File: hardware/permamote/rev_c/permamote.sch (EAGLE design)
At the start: 125 parts, among them J1 TC2030-JLINK-NL, J5 MICRO_USB_B_HIROSE_ZX62R-B-5P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, Q1 PMDXB950UPEL, Q10 PMDXB950UPEL, Q2 PMDXB950UPEL, Q3 PMDXB950UPEL, Q4 PMDXB950UPEL, Q5 PMDXB950UPEL, Q6 PMDXB950UPEL, Q7 PMDXB950UPEL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

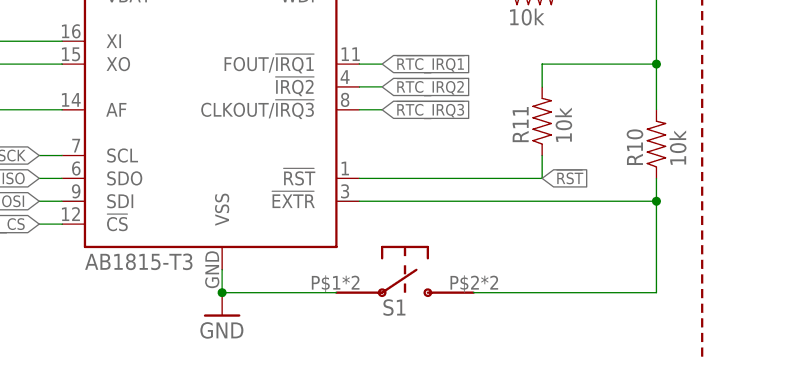
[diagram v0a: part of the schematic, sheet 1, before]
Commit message: Change button, fixes #4
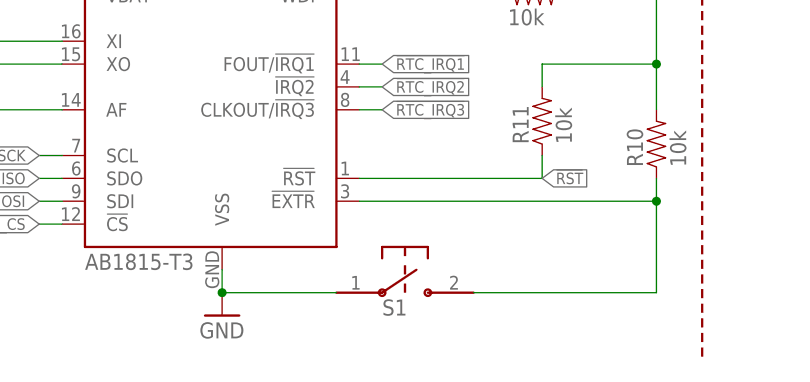
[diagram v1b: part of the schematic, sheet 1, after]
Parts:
- S1: value EVQP2 -> B3U-1000P; device switches:EVQP2 -> switches:B3U-1000P; MPN EVQ-P2K02Q -> (none)
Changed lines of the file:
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@@
 <part name="A2" library="chips" deviceset="ANT3216A063R2400A" device=""/>
 <part name="GND30" library="supply1" library_urn="urn:adsk.eagle:library:371" deviceset="GND" device=""/>
-<part name="S1" library="switches" deviceset="EVQP2" device="">
-<attribute name="MPN" value="EVQ-P2K02Q "/>
-</part>
 <part name="R10" library="passives" deviceset="RESISTOR" device="0402_RES" value="10k">
 <attribute name="DIGIKEY" value="311-10KJRCT-ND "/>
@@
 <attribute name="MPN" value="CL05B821KO5NNNC"/>
 </part>
+<part name="S1" library="switches" deviceset="B3U" device="-1000P"/>
 </parts>
 <sheets>
@@
 <instance part="P+23" gate="G$1" x="190.5" y="160.02"/>
 <instance part="A2" gate="G$1" x="238.76" y="76.2"/>
-<instance part="S1" gate="G$1" x="88.9" y="7.62">
-<attribute name="MPN" x="88.9" y="7.62" size="1.778" layer="96" display="off"/>
-</instance>
 <instance part="R10" gate="G$1" x="116.84" y="25.4" rot="R90">
 <attribute name="DIGIKEY" x="116.84" y="25.4" size="1.778" layer="96" rot="R90" display="off"/>
@@
 <attribute name="MPN" x="88.9" y="139.7" size="1.778" layer="96" display="off"/>
 </instance>
+<instance part="S1" gate="G$1" x="88.9" y="7.62"/>
 </instances>
 <busses>
@@
 <wire x1="68.58" y1="10.16" x2="68.58" y2="7.62" width="0.1524" layer="91"/>
 <pinref part="GND14" gate="1" pin="GND"/>
-<pinref part="S1" gate="G$1" pin="P$1"/>
 <wire x1="68.58" y1="7.62" x2="81.28" y2="7.62" width="0.1524" layer="91"/>
 <junction x="68.58" y="7.62"/>
+<pinref part="S1" gate="G$1" pin="P$1"/>
 </segment>
 <segment>
@@
 <pinref part="U1" gate="G$1" pin="!EXTR"/>
 <wire x1="83.82" y1="17.78" x2="116.84" y2="17.78" width="0.1524" layer="91"/>
-<pinref part="S1" gate="G$1" pin="P$2"/>
 <wire x1="96.52" y1="7.62" x2="116.84" y2="7.62" width="0.1524" layer="91"/>
 <wire x1="116.84" y1="7.62" x2="116.84" y2="17.78" width="0.1524" layer="91"/>
@@
 <wire x1="116.84" y1="17.78" x2="116.84" y2="20.32" width="0.1524" layer="91"/>
 <pinref part="R10" gate="G$1" pin="1"/>
-</segment>
-</net>
+<pinref part="S1" gate="G$1" pin="P$2"/>
+</segment>
+</net>
